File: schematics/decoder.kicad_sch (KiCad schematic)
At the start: 4 parts, among them U4 74HC00, U5 74HC30, U6 74HC04, U7 74HC138

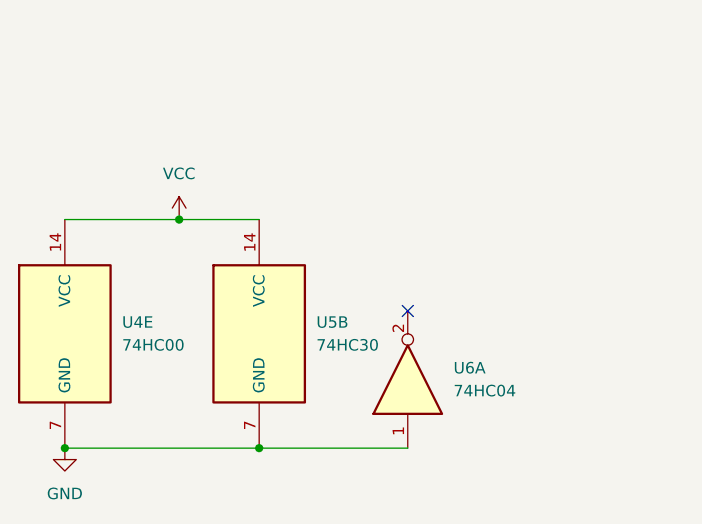
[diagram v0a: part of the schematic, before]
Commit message: trying to make it automatically hold reset during power-on. it's a little better
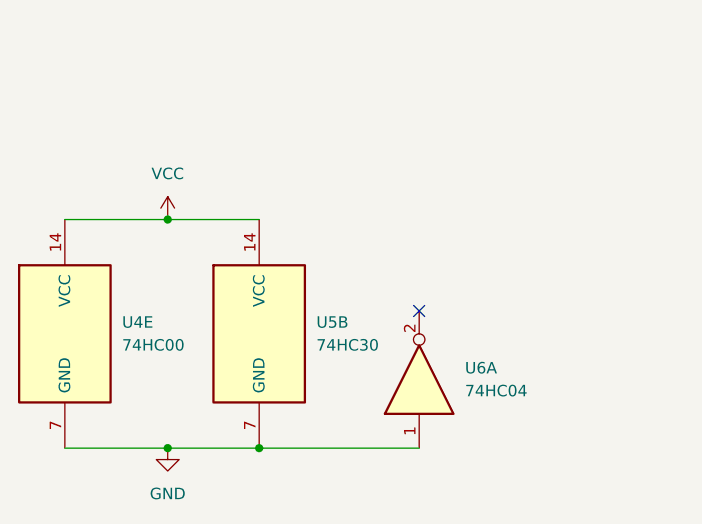
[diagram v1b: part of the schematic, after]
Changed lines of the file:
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@@
 	(paper "USLetter")
+	(junction
+		(at 50.8 191.77)
+		(diameter 0)
+		(color 0 0 0 0)
+	)
+	(junction
+		(at 40.64 191.77)
+		(diameter 0)
+		(color 0 0 0 0)
+	)
 	(junction
 		(at 124.46 106.68)
@@
 	)
 	(junction
+		(at 40.64 166.37)
+		(diameter 0)
+		(color 0 0 0 0)
+	)
+	(junction
 		(at 127 76.2)
 		(diameter 0)
@@
 	)
 	(junction
-		(at 41.91 166.37)
-		(diameter 0)
-		(color 0 0 0 0)
-	)
-	(junction
-		(at 29.21 191.77)
-		(diameter 0)
-		(color 0 0 0 0)
-	)
-	(junction
 		(at 121.92 76.2)
 		(diameter 0)
 		(color 0 0 0 0)
 	)
-	(junction
-		(at 50.8 191.77)
-		(diameter 0)
-		(color 0 0 0 0)
-	)
 	(no_connect
 		(at 127 142.24)
@@
 	)
 	(no_connect
+		(at 68.58 176.53)
+	)
+	(no_connect
 		(at 121.92 142.24)
 	)
 	(no_connect
 		(at 124.46 142.24)
-	)
-	(no_connect
-		(at 67.31 176.53)
 	)
 	(no_connect
@@
 	(wire
 		(pts
-			(xy 41.91 166.37) (xy 50.8 166.37)
-		)
-		(stroke
-			(width 0)
-			(type default)
-		)
-	)
-	(wire
-		(pts
 			(xy 127 76.2) (xy 128.27 76.2)
 		)
@@
 	(wire
 		(pts
+			(xy 40.64 191.77) (xy 29.21 191.77)
+		)
+		(stroke
+			(width 0)
+			(type default)
+		)
+	)
+	(wire
+		(pts
 			(xy 100.33 99.06) (xy 105.41 99.06)
 		)
@@
 	(wire
 		(pts
+			(xy 40.64 166.37) (xy 50.8 166.37)
+		)
+		(stroke
+			(width 0)
+			(type default)
+		)
+	)
+	(wire
+		(pts
 			(xy 100.33 104.14) (xy 105.41 104.14)
 		)
@@
 	(wire
 		(pts
-			(xy 29.21 166.37) (xy 41.91 166.37)
+			(xy 29.21 166.37) (xy 40.64 166.37)
 		)
 		(stroke
@@
 	(wire
 		(pts
-			(xy 50.8 191.77) (xy 67.31 191.77)
-		)
-		(stroke
-			(width 0)
-			(type default)
-		)
-	)
-	(wire
-		(pts
 			(xy 100.33 116.84) (xy 114.3 116.84)
 		)
@@
 	(wire
 		(pts
-			(xy 50.8 191.77) (xy 29.21 191.77)
+			(xy 50.8 191.77) (xy 40.64 191.77)
 		)
 		(stroke
@@
 		(pts
 			(xy 111.76 119.38) (xy 111.76 121.92)
+		)
+		(stroke
+			(width 0)
+			(type default)
+		)
+	)
+	(wire
+		(pts
+			(xy 50.8 191.77) (xy 68.58 191.77)
 		)
 		(stroke
@@
 					(reference "U6")
 					(unit 3)
-				)
-			)
-		)
-	)
-	(symbol
-		(lib_id "74xx:74HC04")
-		(at 67.31 184.15 90)
-		(unit 1)
-		(body_style 1)
-		(exclude_from_sim no)
-		(in_bom yes)
-		(on_board yes)
-		(in_pos_files yes)
-		(dnp no)
-		(fields_autoplaced yes)
-		(property "Reference" "U6"
-			(at 72.39 182.8799 90)
-			(show_name no)
-			(do_not_autoplace no)
-			(effects
-				(font
-					(size 1.27 1.27)
-				)
-				(justify right)
-			)
-		)
-		(property "Value" "74HC04"
-			(at 72.39 185.4199 90)
-			(show_name no)
-			(do_not_autoplace no)
-			(effects
-				(font
-					(size 1.27 1.27)
-				)
-				(justify right)
-			)
-		)
-		(property "Footprint" ""
-			(at 67.31 184.15 0)
-			(hide yes)
-			(show_name no)
-			(do_not_autoplace no)
-			(effects
-				(font
-					(size 1.27 1.27)
-				)
-			)
-		)
-		(property "Datasheet" "https://assets.nexperia.com/documents/data-sheet/74HC_HCT04.pdf"
-			(at 67.31 184.15 0)
-			(hide yes)
-			(show_name no)
-			(do_not_autoplace no)
-			(effects
-				(font
-					(size 1.27 1.27)
-				)
-			)
-		)
-		(property "Description" "Hex Inverter"
-			(at 67.31 184.15 0)
-			(hide yes)
-			(show_name no)
-			(do_not_autoplace no)
-			(effects
-				(font
-					(size 1.27 1.27)
-				)
-			)
-		)
-		(pin "11"
-		)
-		(pin "12"
-		)
-		(pin "14"
-		)
-		(pin "10"
-		)
-		(pin "7"
-		)
-		(pin "13"
-		)
-		(pin "1"
-		)
-		(pin "8"
-		)
-		(pin "2"
-		)
-		(pin "3"
-		)
-		(pin "4"
-		)
-		(pin "5"
-		)
-		(pin "6"
-		)
-		(pin "9"
-		)
-		(instances
-			(project "bv6502_hw"
-				(path "/94c72abe-aaa5-49aa-8ab7-5d3e7cbc10be/84bb5624-3de3-475d-b983-481178beada9"
-					(reference "U6")
-					(unit 1)
 				)
 			)
@@
 	(symbol
 		(lib_id "power:GND")
-		(at 29.21 191.77 0)
+		(at 40.64 191.77 0)
 		(unit 1)
 		(body_style 1)
@@
 		(fields_autoplaced yes)
 		(property "Reference" "#PWR011"
-			(at 29.21 198.12 0)
+			(at 40.64 198.12 0)
 			(hide yes)
 			(show_name no)
@@
 		)
 		(property "Value" "GND"
-			(at 29.21 196.85 0)
+			(at 40.64 196.85 0)
 			(show_name no)
 			(do_not_autoplace no)
@@
 		)
 		(property "Footprint" ""
-			(at 29.21 191.77 0)
+			(at 40.64 191.77 0)
 			(hide yes)
 			(show_name no)
@@
 		)
 		(property "Datasheet" ""
-			(at 29.21 191.77 0)
+			(at 40.64 191.77 0)
 			(hide yes)
 			(show_name no)
@@
 		)
 		(property "Description" "Power symbol creates a global label with name \"GND\" , ground"
-			(at 29.21 191.77 0)
+			(at 40.64 191.77 0)
 			(hide yes)
 			(show_name no)
@@
 	(symbol
 		(lib_id "power:VCC")
-		(at 41.91 166.37 0)
+		(at 40.64 166.37 0)
 		(unit 1)
 		(body_style 1)
@@
 		(fields_autoplaced yes)
 		(property "Reference" "#PWR012"
-			(at 41.91 170.18 0)
+			(at 40.64 170.18 0)
 			(hide yes)
 			(show_name no)
@@
 		)
 		(property "Value" "VCC"
-			(at 41.91 161.29 0)
+			(at 40.64 161.29 0)
 			(show_name no)
 			(do_not_autoplace no)
@@
 		)
 		(property "Footprint" ""
-			(at 41.91 166.37 0)
+			(at 40.64 166.37 0)
 			(hide yes)
 			(show_name no)
@@
 		)
 		(property "Datasheet" ""
-			(at 41.91 166.37 0)
+			(at 40.64 166.37 0)
 			(hide yes)
 			(show_name no)
@@
 		)
 		(property "Description" "Power symbol creates a global label with name \"VCC\""
-			(at 41.91 166.37 0)
+			(at 40.64 166.37 0)
 			(hide yes)
 			(show_name no)
@@
 				)
 			)
+		)
+	)
+	(symbol
+		(lib_id "74xx:74HC04")
+		(at 68.58 184.15 90)
+		(unit 1)
+		(body_style 1)
+		(exclude_from_sim no)
+		(in_bom yes)
+		(on_board yes)
+		(in_pos_files yes)
+		(dnp no)
+		(fields_autoplaced yes)
+		(property "Reference" "U6"
+			(at 73.66 182.8799 90)
+			(show_name no)
+			(do_not_autoplace no)
+			(effects
+				(font
+					(size 1.27 1.27)
+				)
+				(justify right)
+			)
+		)
+		(property "Value" "74HC04"
+			(at 73.66 185.4199 90)
+			(show_name no)
+			(do_not_autoplace no)
+			(effects
+				(font
+					(size 1.27 1.27)
+				)
+				(justify right)
+			)
+		)
+		(property "Footprint" ""
+			(at 68.58 184.15 0)
+			(hide yes)
+			(show_name no)
+			(do_not_autoplace no)
+			(effects
+				(font
+					(size 1.27 1.27)
+				)
+			)
+		)
+		(property "Datasheet" "https://assets.nexperia.com/documents/data-sheet/74HC_HCT04.pdf"
+			(at 68.58 184.15 0)
+			(hide yes)
+			(show_name no)
+			(do_not_autoplace no)
+			(effects
+				(font
+					(size 1.27 1.27)
+				)
+			)
+		)
+		(property "Description" "Hex Inverter"
+			(at 68.58 184.15 0)
+			(hide yes)
+			(show_name no)
+			(do_not_autoplace no)
+			(effects
+				(font
+					(size 1.27 1.27)
+				)
+			)
+		)
+		(pin "11"
+		)
+		(pin "12"
+		)
+		(pin "14"
+		)
+		(pin "10"
+		)
+		(pin "7"
+		)
+		(pin "13"
+		)
+		(pin "1"
+		)
+		(pin "8"
+		)
+		(pin "2"
+		)
+		(pin "3"
+		)
+		(pin "4"
+		)
+		(pin "5"
+		)
+		(pin "6"
+		)
+		(pin "9"
+		)
+		(instances
+			(project "bv6502_hw"
+				(path "/94c72abe-aaa5-49aa-8ab7-5d3e7cbc10be/84bb5624-3de3-475d-b983-481178beada9"
+					(reference "U6")
+					(unit 1)
+				)
+			)

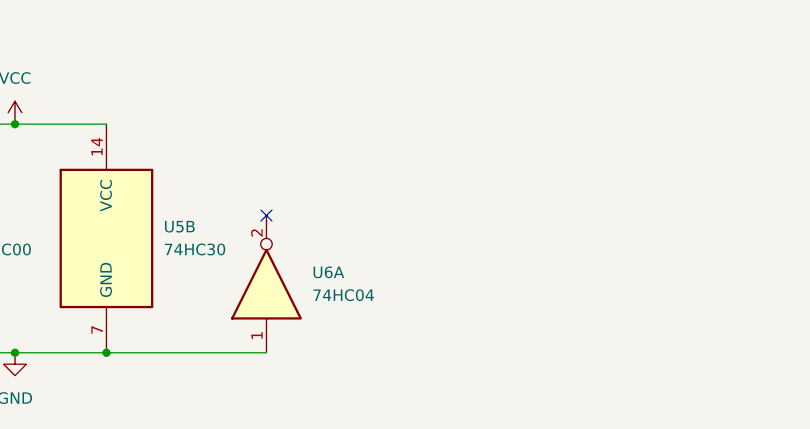
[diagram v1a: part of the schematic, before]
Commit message: removed unnecessary clock inversion
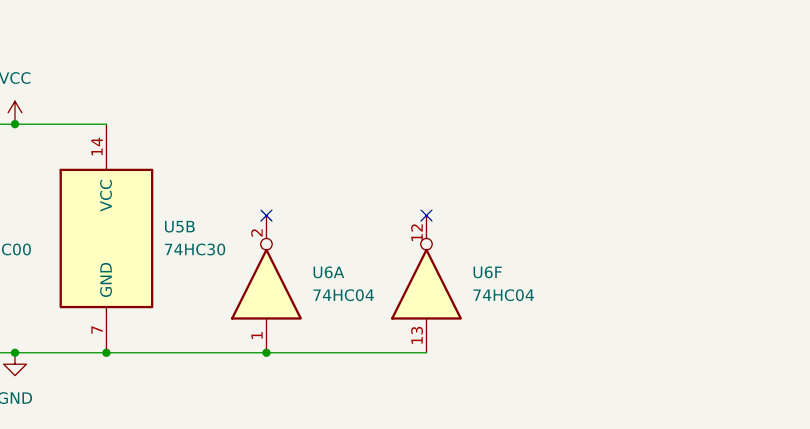
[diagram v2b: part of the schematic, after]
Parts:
- added unit 6 of U6
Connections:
- net GND: now also U6.13
- no-connect marks 7 -> 8
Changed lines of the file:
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@@
+	)
+	(junction
+		(at 68.58 191.77)
+		(diameter 0)
+		(color 0 0 0 0)
 	)
 	(junction
@@
 	)
 	(no_connect
+		(at 86.36 176.53)
+	)
+	(no_connect
 		(at 121.92 142.24)
 	)
@@
 		(pts
 			(xy 124.46 106.68) (xy 124.46 121.92)
+		)
+		(stroke
+			(width 0)
+			(type default)
+		)
+	)
+	(wire
+		(pts
+			(xy 68.58 191.77) (xy 86.36 191.77)
 		)
 		(stroke
@@
 			)
 		)
+	)
+	(symbol
+		(lib_id "74xx:74HC04")
+		(at 86.36 184.15 90)
+		(unit 6)
+		(body_style 1)
+		(exclude_from_sim no)
+		(in_bom yes)
+		(on_board yes)
+		(in_pos_files yes)
+		(dnp no)
+		(fields_autoplaced yes)
+		(property "Reference" "U6"
+			(at 91.44 182.8799 90)
+			(show_name no)
+			(do_not_autoplace no)
+			(effects
+				(font
+					(size 1.27 1.27)
+				)
+				(justify right)
+			)
+		)
+		(property "Value" "74HC04"
+			(at 91.44 185.4199 90)
+			(show_name no)
+			(do_not_autoplace no)
+			(effects
+				(font
+					(size 1.27 1.27)
+				)
+				(justify right)
+			)
+		)
+		(property "Footprint" ""
+			(at 86.36 184.15 0)
+			(hide yes)
+			(show_name no)
+			(do_not_autoplace no)
+			(effects
+				(font
+					(size 1.27 1.27)
+				)
+			)
+		)
+		(property "Datasheet" "https://assets.nexperia.com/documents/data-sheet/74HC_HCT04.pdf"
+			(at 86.36 184.15 0)
+			(hide yes)
+			(show_name no)
+			(do_not_autoplace no)
+			(effects
+				(font
+					(size 1.27 1.27)
+				)
+			)
+		)
+		(property "Description" "Hex Inverter"
+			(at 86.36 184.15 0)
+			(hide yes)
+			(show_name no)
+			(do_not_autoplace no)
+			(effects
+				(font
+					(size 1.27 1.27)
+				)
+			)
+		)
+		(pin "11"
+		)
+		(pin "12"
+		)
+		(pin "14"
+		)
+		(pin "10"
+		)
+		(pin "7"
+		)
+		(pin "13"
+		)
+		(pin "1"
+		)
+		(pin "8"
+		)
+		(pin "2"
+		)
+		(pin "3"
+		)
+		(pin "4"
+		)
+		(pin "5"
+		)
+		(pin "6"
+		)
+		(pin "9"
+		)
+		(instances
+			(project "bv6502_hw"
+				(path "/94c72abe-aaa5-49aa-8ab7-5d3e7cbc10be/84bb5624-3de3-475d-b983-481178beada9"
+					(reference "U6")
+					(unit 6)
+				)
+			)
+		)

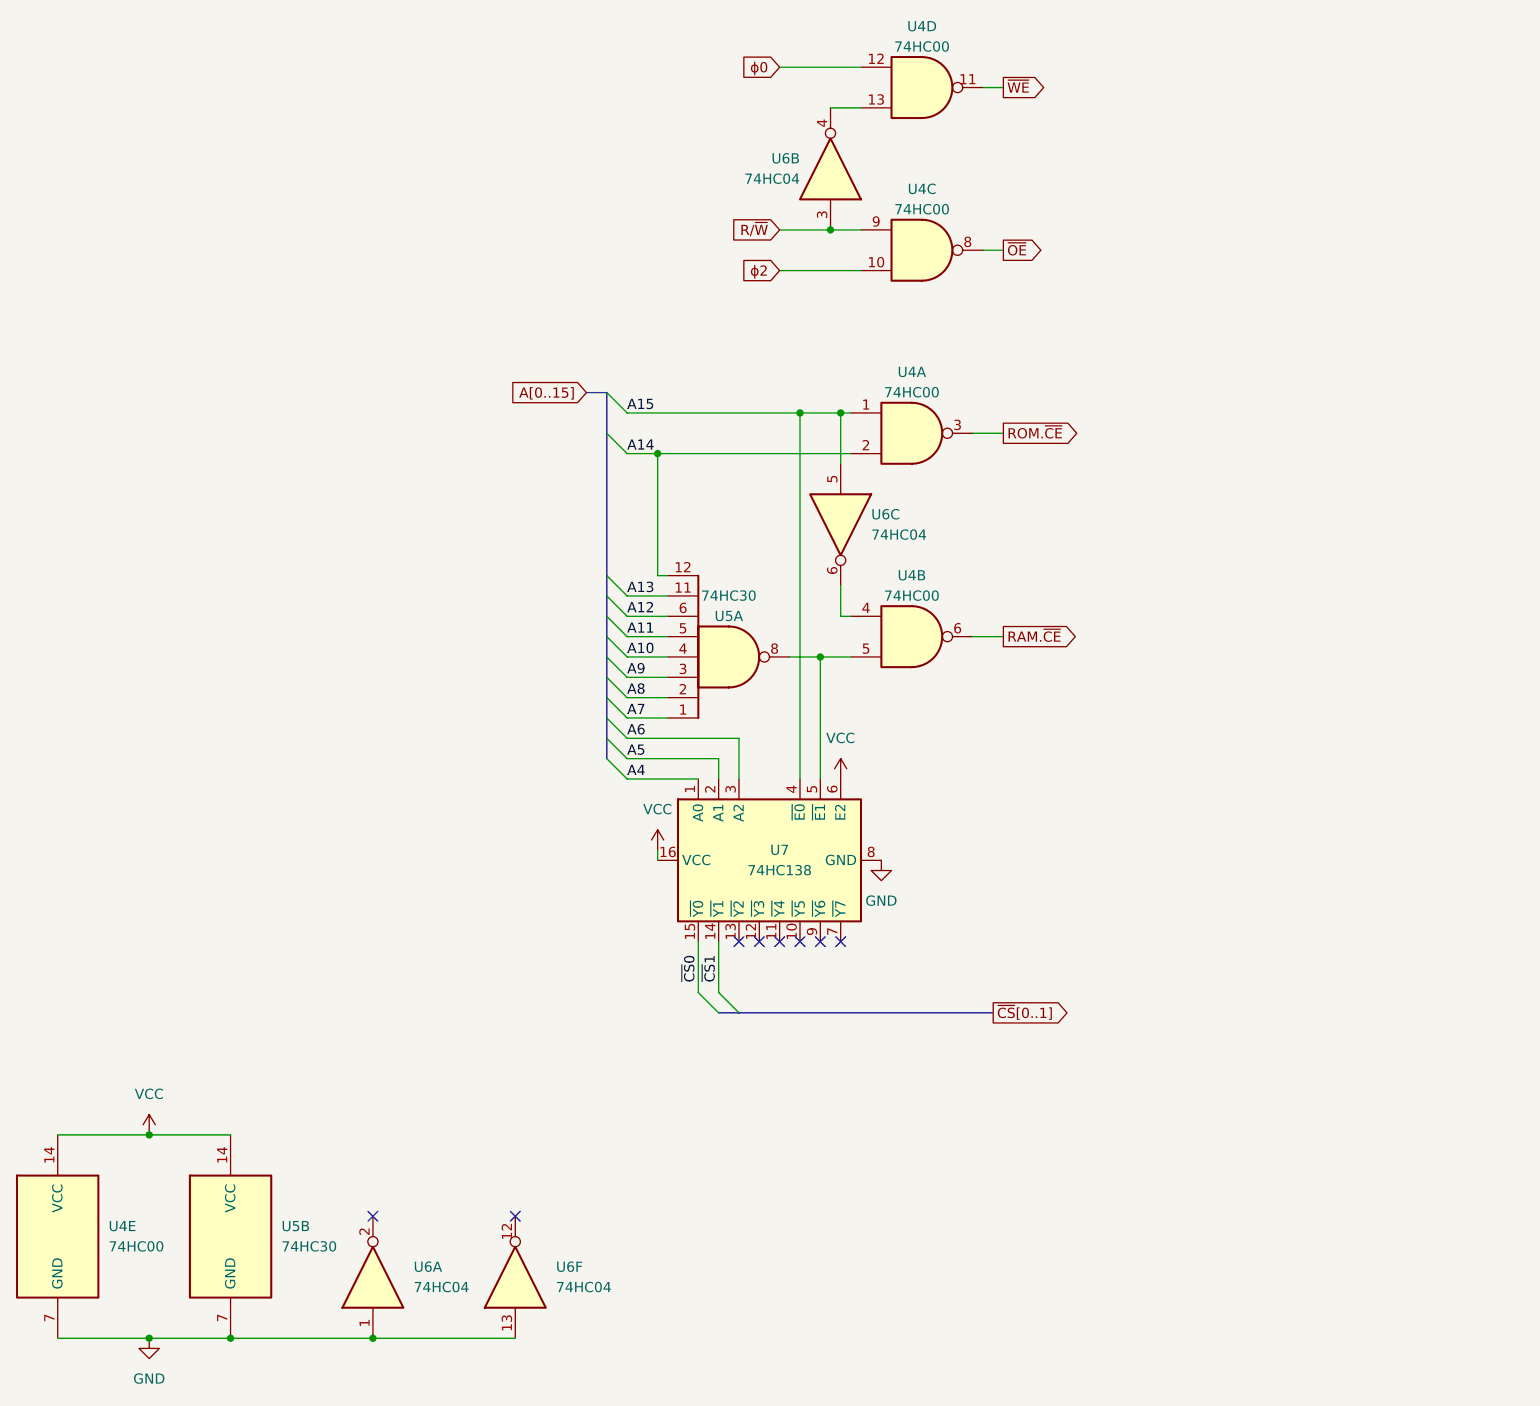
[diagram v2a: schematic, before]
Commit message: Address decoder pld file and no-VIA keyboard schematic and pld file.
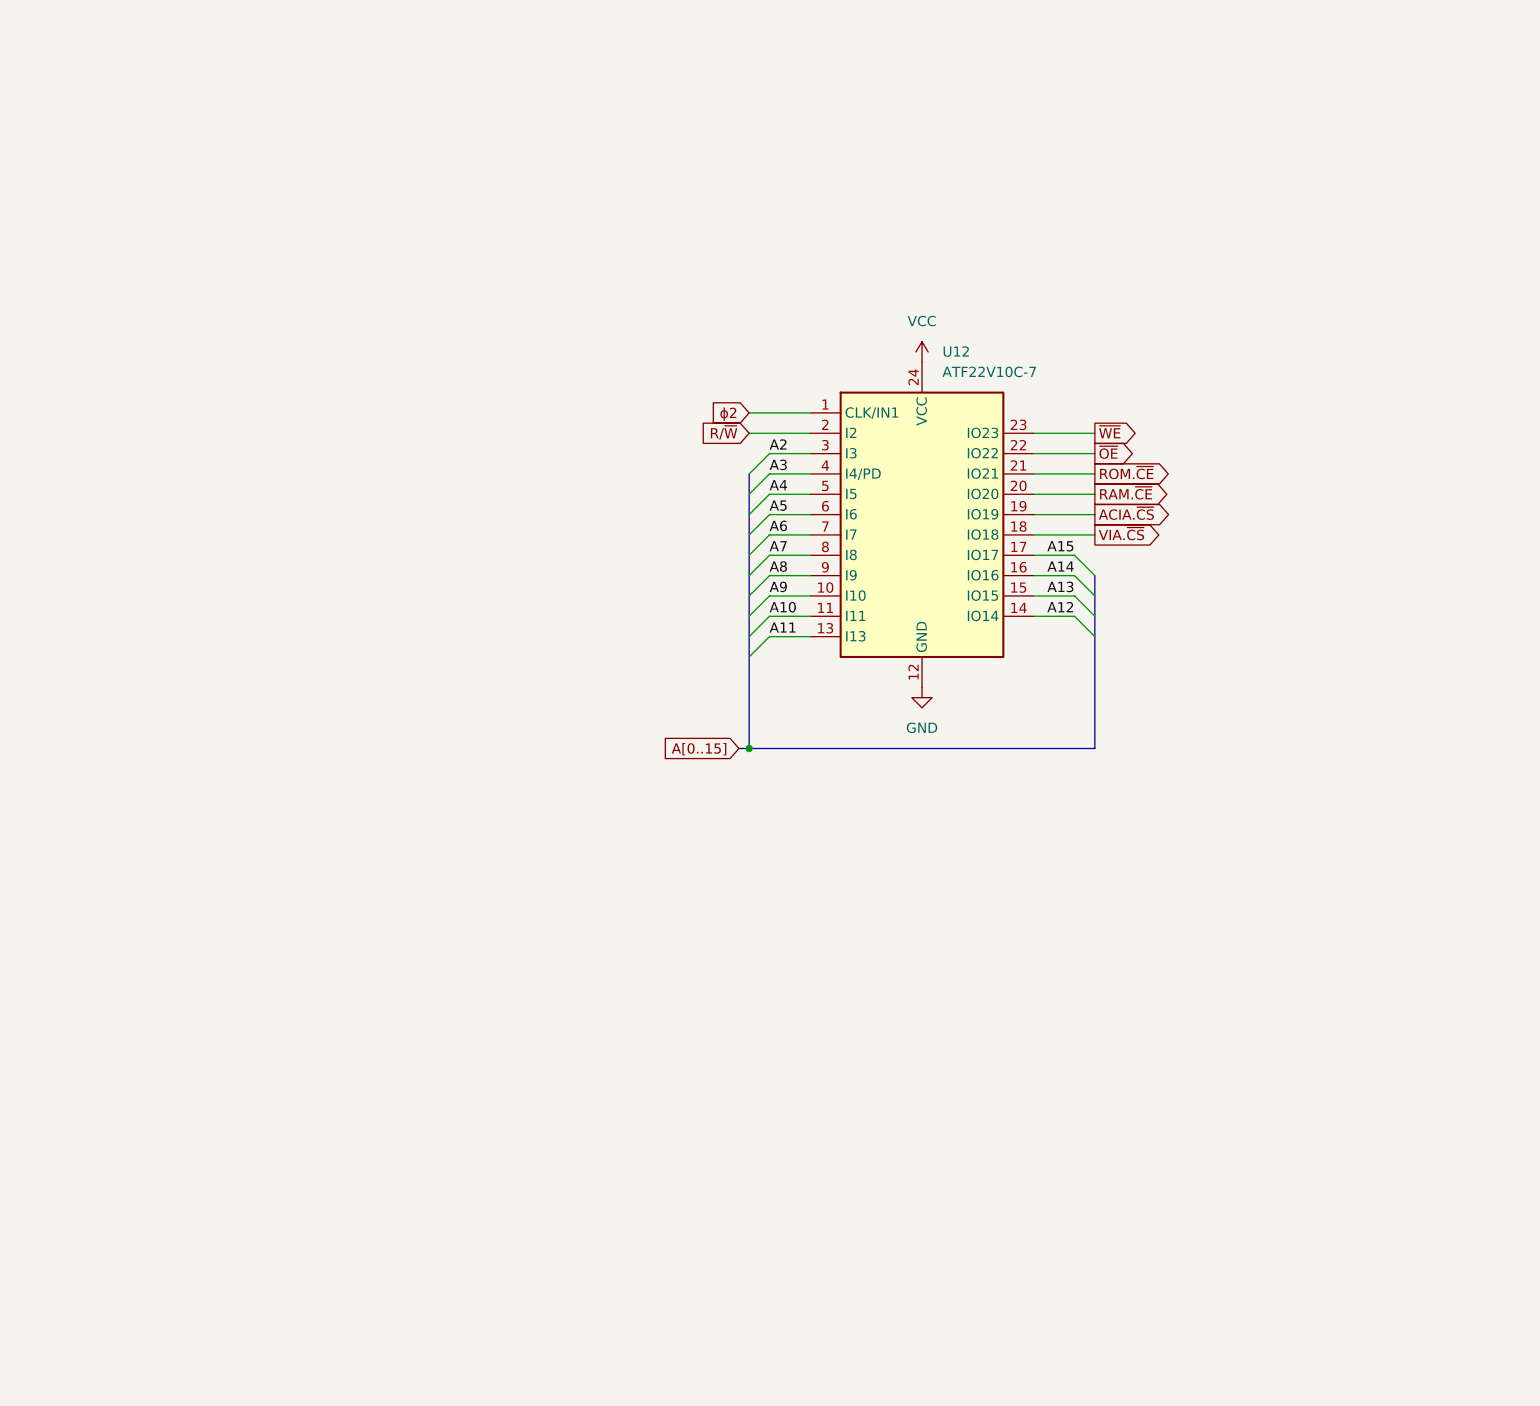
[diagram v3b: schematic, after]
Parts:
- removed U4: 74HC00, symbol 74xx:74HC00
- removed U5: 74HC30, symbol 74xx:74LS30
- removed U6: 74HC04, symbol 74xx:74HC04
- removed U7: 74HC138, symbol 74xx:74HC138
- added U12: ATF22V10C-7, Package_DIP:DIP-24_W7.62mm, symbol Logic_Programmable:PEEL22CV10AP
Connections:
- net A10: now also U12.11 (I11)
- net A11: now also U12.13 (I13)
- net A12: now also U12.14 (IO14)
- net A13: now also U12.15 (IO15)
- net A14: now also U12.16 (IO16)
- net A15: now also U12.17 (IO17)
- net A4: now also U12.5 (I5)
- net A5: now also U12.6 (I6)
- net A6: now also U12.7 (I7)
- net A7: now also U12.8 (I8)
- net A8: now also U12.9 (I9)
- net A9: now also U12.10 (I10)
- net GND: now also U12.12 (GND)
- net RAM.~{CE}: now also U12.20 (IO20)
- net ROM.~{CE}: now also U12.21 (IO21)
- net R/~{W}: now also U12.2 (I2)
- net VCC: now also U12.24 (VCC)
- net ~{OE}: now also U12.22 (IO22)
- net ~{WE}: now also U12.23 (IO23)
- net ϕ2: now also U12.1 (CLK/IN1)
- new net A2: U12.3 (I3)
- new net A3: U12.4 (I4/PD)
- new net ACIA.~{CS}: U12.19 (IO19)
- new net VIA.~{CS}: U12.18 (IO18)
- no-connect marks 8 -> 0
